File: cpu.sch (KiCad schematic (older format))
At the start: 21 parts, among them U1 68000D, U10 74LS244, U11 74LS373, U12 74LS244, U13 74LS373, U2 FAT_AGNUS_8375, U37 74LS32, U5 GARY_5719

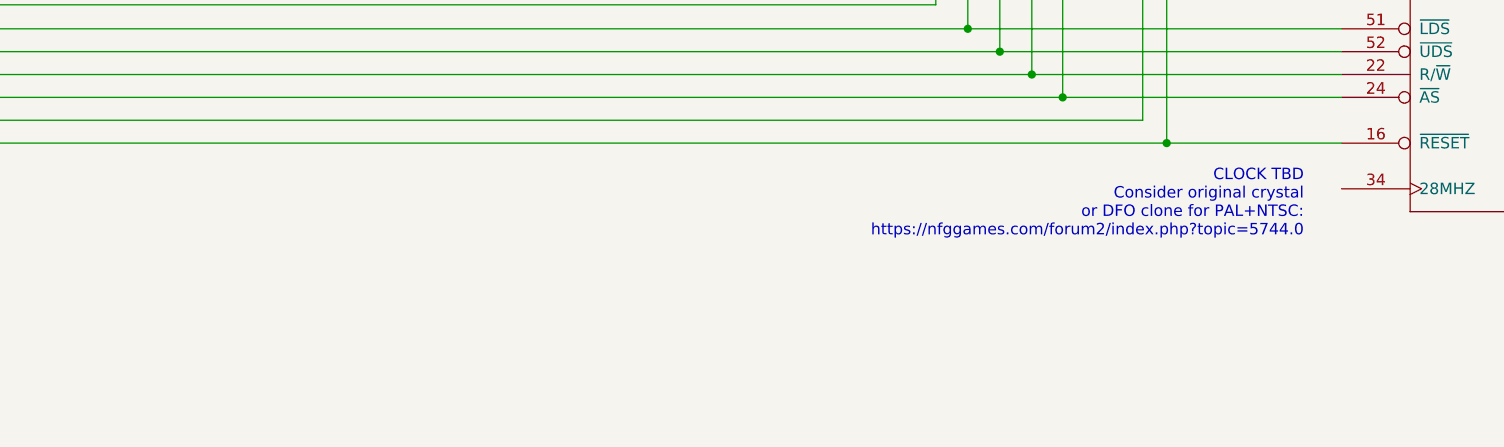
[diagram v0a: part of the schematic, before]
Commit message: Add main crystal
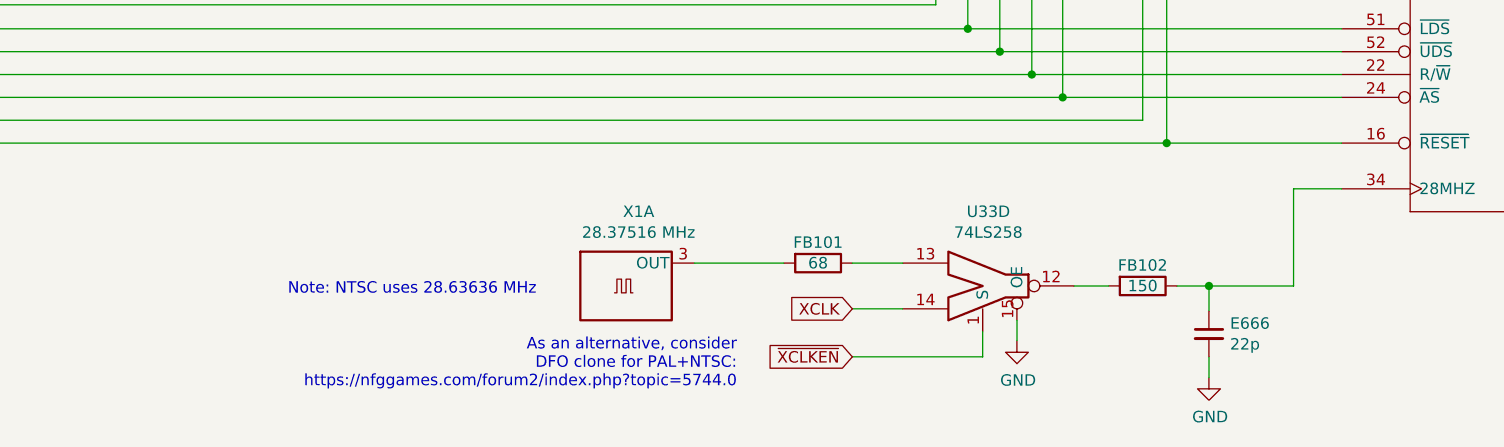
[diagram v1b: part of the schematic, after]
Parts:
- added E666: 22p, symbol Device:C_Small
- added FB101: 68, symbol Device:R
- added FB102: 150, symbol Device:R
- added U33: 74LS258, symbol 74ls258:74LS258
- added X1: 28.37516 MHz, Oscillator:Oscillator_SMD_TXC_7C-4Pin_5.0x3.2mm, symbol xtal:XTAL
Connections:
- net GND: now also E666.2, U33.15 (OE)
- net at U2.34 (28MHZ): now also E666.1, FB102.1
- new net: FB102.2, U33.12
- new net: FB101.1, U33.13
- new net: FB101.2, X1.3 (OUT)
- new net XCLK: U33.14
- new net ~XCLKEN: U33.1 (S)
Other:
- note added: "As an alternative, consider\nDFO clone for PAL+NTSC:\nhttps://nfggames.com/forum2/index.php?topic=5744.0"
- note added: "Note: NTSC uses 28.63636 MHz"
- note removed: "CLOCK TBD\nConsider original crystal\nor DFO clone for PAL+NTSC:\nhttps://nfggames.com/forum2/index.php?topic=5744.0"
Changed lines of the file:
@@
 Text GLabel 1140 3735 0    50   BiDi ~ 0
 FC[0..2]
-Text Notes 10015 10050 2    50   ~ 0
-CLOCK TBD\nConsider original crystal\nor DFO clone for PAL+NTSC:\nhttps://nfggames.com/forum2/index.php?topic=5744.0
+Text Notes 7535 10710 2    50   ~ 0
+As an alternative, consider\nDFO clone for PAL+NTSC:\nhttps://nfggames.com/forum2/index.php?topic=5744.0
 Text Label 12980 6335 2    50   ~ 0
 dra9
@@
 Text Label 10140 8135 2    50   ~ 0
 drd8
-Wire Bus Line
-	1370 3735 1370 3935
-Wire Bus Line
-	1370 3235 1370 3435
-Wire Bus Line
-	13405 5535 13405 6235
-Wire Bus Line
-	13405 6435 13405 7335
-Wire Bus Line
-	9645 7335 9645 8835
-Wire Bus Line
-	5325 590  5325 4785
-Wire Bus Line
-	9645 590  9645 7135
-Wire Bus Line
-	5610 710  5610 7035
-Wire Bus Line
-	8110 825  8110 7335
 Text Label 13425 6235 0    50   ~ 0
 rga[1..8]
@@
 Text Label 1675 4035 0    50   ~ 0
 fc0
+$Comp
+L 74ls258:74LS258 U33
+U 4 1 5CBE9A78
+P 8610 10260
+F 0 "U33" H 8635 10585 50  0000 C CNN
+F 1 "74LS258" H 8635 10494 50  0000 C CNN
+F 2 "" H 11710 7960 50  0001 C CNN
+F 3 "http://www.ti.com/lit/gpn/sn74LS258" H 11710 7960 50  0001 C CNN
+	4    8610 10260
+	1    0    0    -1
+$EndComp
+Wire Wire Line
+	9010 10260 9160 10260
+$Comp
+L Device:R FB102
+U 1 1 5CC23FBE
+P 9310 10260
+F 0 "FB102" V 9220 10260 50  0000 C CNN
+F 1 "150" V 9310 10260 50  0000 C CNN
+F 2 "" V 9240 10260 50  0001 C CNN
+F 3 "~" H 9310 10260 50  0001 C CNN
+	1    9310 10260
+	0    1    1    0
+$EndComp
+Wire Wire Line
+	9460 10260 9600 10260
+$Comp
+L Device:C_Small E666
+U 1 1 5CC5EA40
+P 9600 10470
+F 0 "E666" H 9692 10516 50  0000 L CNN
+F 1 "22p" H 9692 10425 50  0000 L CNN
+F 2 "" H 9600 10470 50  0001 C CNN
+F 3 "~" H 9600 10470 50  0001 C CNN
+	1    9600 10470
+	1    0    0    -1
+$EndComp
+Wire Wire Line
+	9600 10370 9600 10260
+Connection ~ 9600 10260
+Wire Wire Line
+	9600 10570 9600 10660
+$Comp
+L power:GND #PWR?
+U 1 1 5CD0F28E
+P 9600 10660
+F 0 "#PWR?" H 9600 10410 50  0001 C CNN
+F 1 "GND" H 9605 10487 50  0000 C CNN
+F 2 "" H 9600 10660 50  0001 C CNN
+F 3 "" H 9600 10660 50  0001 C CNN
+	1    9600 10660
+	1    0    0    -1
+$EndComp
+Wire Wire Line
+	8260 10360 8040 10360
+Text GLabel 8040 10360 0    50   Input ~ 0
+XCLK
+Wire Wire Line
+	8260 10160 8040 10160
+$Comp
+L Device:R FB101
+U 1 1 5CD85D7B
+P 7890 10160
+F 0 "FB101" V 7800 10160 50  0000 C CNN
+F 1 "68" V 7890 10160 50  0000 C CNN
+F 2 "" V 7820 10160 50  0001 C CNN
+F 3 "~" H 7890 10160 50  0001 C CNN
+	1    7890 10160
+	0    1    1    0
+$EndComp
+Text GLabel 8040 10570 0    50   Input ~ 0
+~XCLKEN
+Wire Wire Line
+	8610 10570 8610 10460
+Wire Wire Line
+	8040 10570 8610 10570
+Wire Wire Line
+	8760 10410 8760 10500
+$Comp
+L power:GND #PWR?
+U 1 1 5CEEE65E
+P 8760 10500
+F 0 "#PWR?" H 8760 10250 50  0001 C CNN
+F 1 "GND" H 8765 10327 50  0000 C CNN
+F 2 "" H 8760 10500 50  0001 C CNN
+F 3 "" H 8760 10500 50  0001 C CNN
+	1    8760 10500
+	1    0    0    -1
+$EndComp
+Wire Wire Line
+	7350 10160 7740 10160
+$Comp
+L xtal:XTAL X1
+U 1 1 5D05A737
+P 7050 10260
+F 0 "X1" H 7105 10585 50  0000 C CNN
+F 1 "28.37516 MHz" H 7105 10494 50  0000 C CNN
+F 2 "Oscillator:Oscillator_SMD_TXC_7C-4Pin_5.0x3.2mm" H 7150 9610 50  0001 C CNN
+F 3 "http://www.txccorp.com/download/products/osc/7C_o.pdf" H 6950 10260 50  0001 C CNN
+	1    7050 10260
+	1    0    0    -1
+$EndComp
+Wire Wire Line
+	9970 10260 9970 9835
+Wire Wire Line
+	9970 9835 10180 9835
+Wire Wire Line
+	9600 10260 9970 10260
+Wire Bus Line
+	1370 3235 1370 3435
+Wire Bus Line
+	1370 3735 1370 3935
+Wire Bus Line
+	13405 5535 13405 6235
+Wire Bus Line
+	13405 6435 13405 7335
+Wire Bus Line
+	9645 7335 9645 8835
+Wire Bus Line
+	5325 590  5325 4785
+Wire Bus Line
+	9645 590  9645 7135
+Wire Bus Line
+	8110 825  8110 7335
+Wire Bus Line
+	5610 710  5610 7035
+Text Notes 5570 10305 0    50   ~ 0
+Note: NTSC uses 28.63636 MHz
 $EndSCHEMATC

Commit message: Add video power
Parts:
- U33: footprint (none) -> Package_DIP:DIP-16_W7.62mm_Socket_LongPads
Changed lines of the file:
@@
 F 0 "U33" H 8635 10585 50  0000 C CNN
 F 1 "74LS258" H 8635 10494 50  0000 C CNN
-F 2 "" H 11710 7960 50  0001 C CNN
+F 2 "Package_DIP:DIP-16_W7.62mm_Socket_LongPads" H 11710 7960 50  0001 C CNN
 F 3 "http://www.ti.com/lit/gpn/sn74LS258" H 11710 7960 50  0001 C CNN
 	4    8610 10260

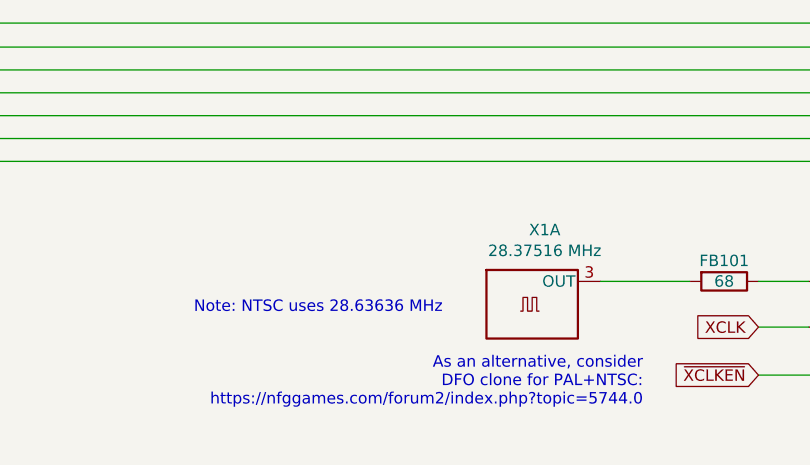
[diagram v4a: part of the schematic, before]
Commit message: Add power & decoupling, not yet complete
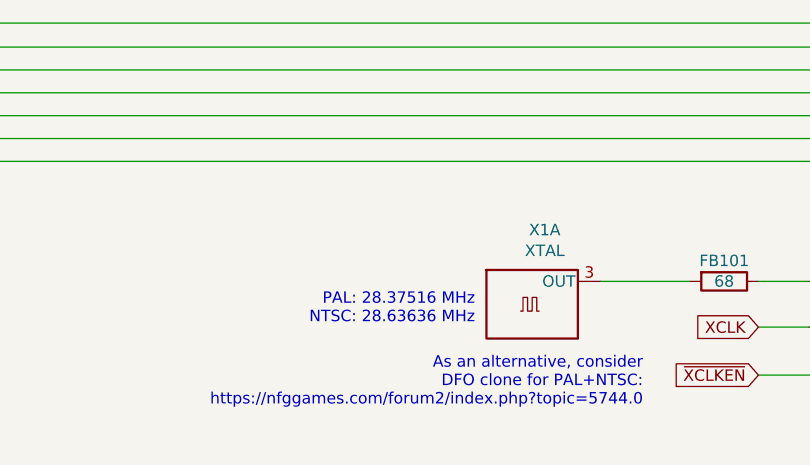
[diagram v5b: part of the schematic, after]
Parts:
- X1: value 28.37516 MHz -> XTAL
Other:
- note added: "PAL: 28.37516 MHz\nNTSC: 28.63636 MHz"
- note removed: "Note: NTSC uses 28.63636 MHz"
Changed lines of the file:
@@
 $Descr A3 16535 11693
 encoding utf-8
-Sheet 2 11
+Sheet 2 12
 Title "Rämixx500"
 Date "2019-04-11"
@@
 P 7050 10260
 F 0 "X1" H 7105 10585 50  0000 C CNN
-F 1 "28.37516 MHz" H 7105 10494 50  0000 C CNN
+F 1 "XTAL" H 7105 10494 50  0000 C CNN
 F 2 "Oscillator:Oscillator_SMD_TXC_7C-4Pin_5.0x3.2mm" H 7150 9610 50  0001 C CNN
 F 3 "http://www.txccorp.com/download/products/osc/7C_o.pdf" H 6950 10260 50  0001 C CNN
@@
 Wire Wire Line
 	9600 10260 9970 10260
+Text Notes 6800 10350 2    50   ~ 0
+PAL: 28.37516 MHz\nNTSC: 28.63636 MHz
 Wire Bus Line
 	1370 3235 1370 3435
@@
 Wire Bus Line
 	5610 710  5610 7035
-Text Notes 5570 10305 0    50   ~ 0
-Note: NTSC uses 28.63636 MHz
 $EndSCHEMATC

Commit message: Add RTC
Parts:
- JP2: footprint (none) -> Raemixx500:Jumper3-Bridged23
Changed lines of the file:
@@
 $Descr A3 16535 11693
 encoding utf-8
-Sheet 2 12
+Sheet 2 13
 Title "Rämixx500"
 Date "2019-04-11"
@@
 F 0 "JP2" V 9900 4952 50  0000 L CNN
 F 1 "Jumper_3_Bridged23" V 9855 4951 50  0001 L CNN
-F 2 "" H 9900 4885 50  0001 C CNN
+F 2 "Raemixx500:Jumper3-Bridged23" H 9900 4885 50  0001 C CNN
 F 3 "~" H 9900 4885 50  0001 C CNN
 	1    9900 4885

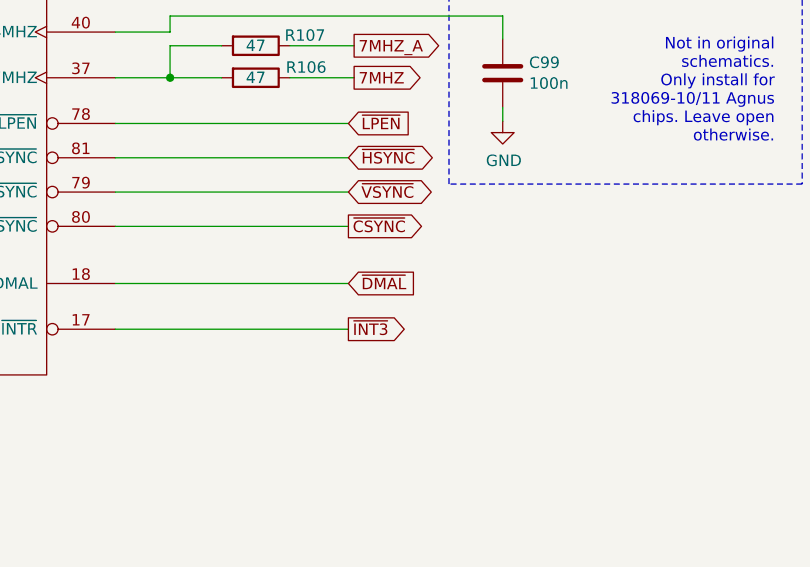
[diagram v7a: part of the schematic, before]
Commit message: Fix power-up reset
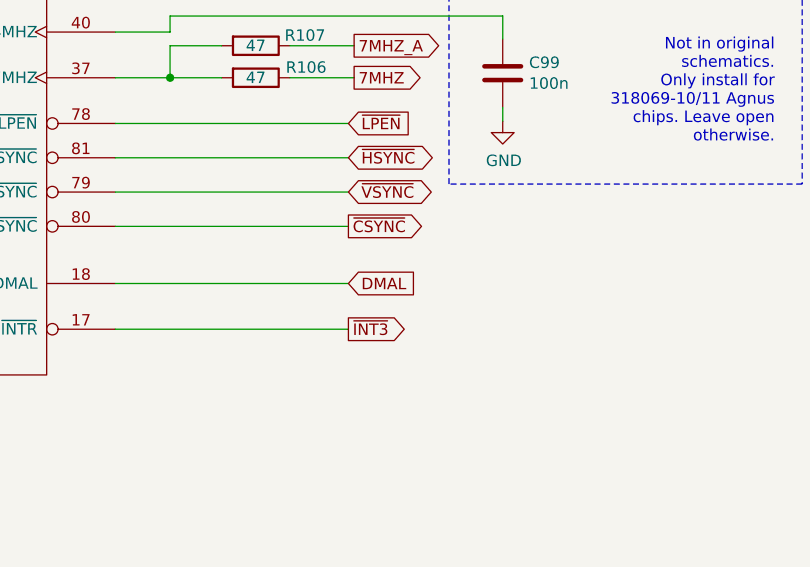
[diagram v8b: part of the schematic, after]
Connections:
- net ~DMAL renamed DMAL
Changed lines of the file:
@@
 EESchema Schematic File Version 4
 LIBS:Raemix500-cache
-EELAYER 26 0
+EELAYER 29 0
 EELAYER END
 $Descr A3 16535 11693
@@
 	12780 9285 13800 9285
 Text GLabel 13800 9535 2    50   Input ~ 0
-~DMAL
+DMAL
 Wire Wire Line
 	12780 9535 13800 9535
